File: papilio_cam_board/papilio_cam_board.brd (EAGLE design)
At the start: 68.4 x 68.6 mm, 20 parts, among them U2 V_REG_317SMD

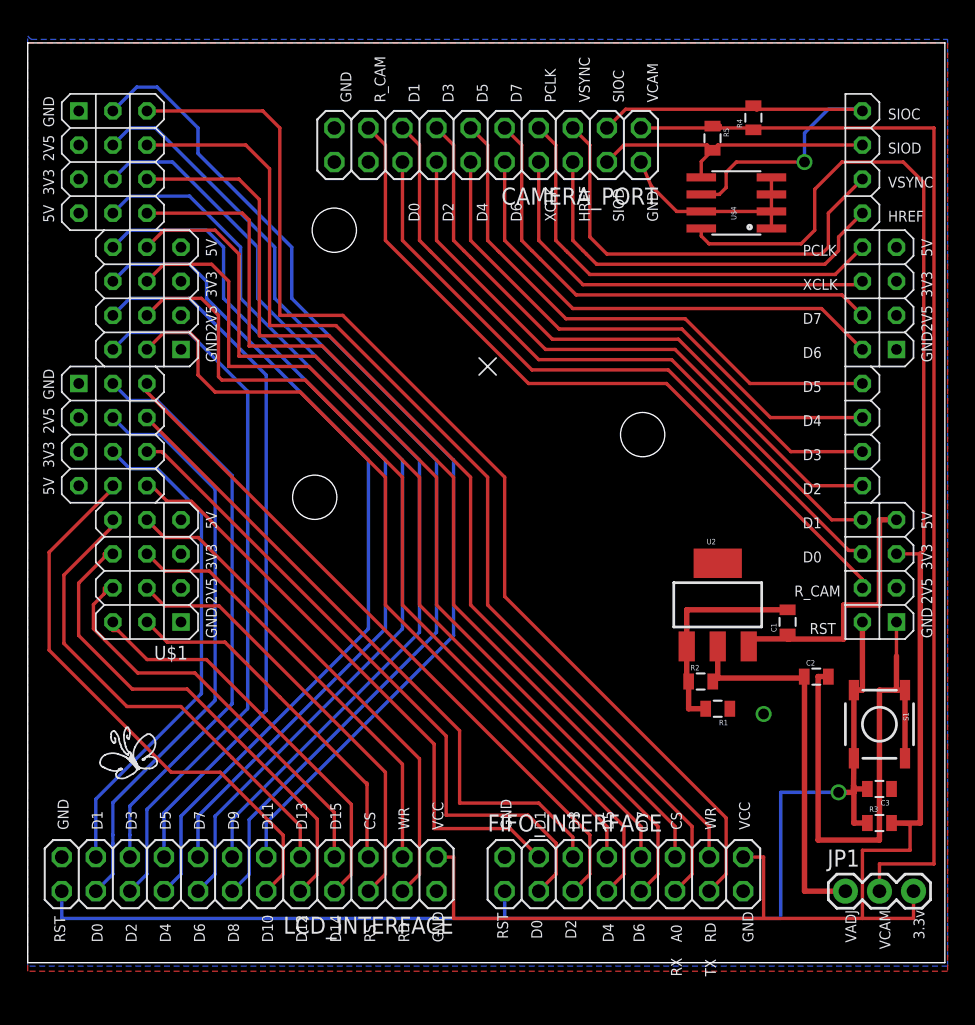
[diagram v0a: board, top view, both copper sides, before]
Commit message: adding papilio wing to support camera sensor and other ports
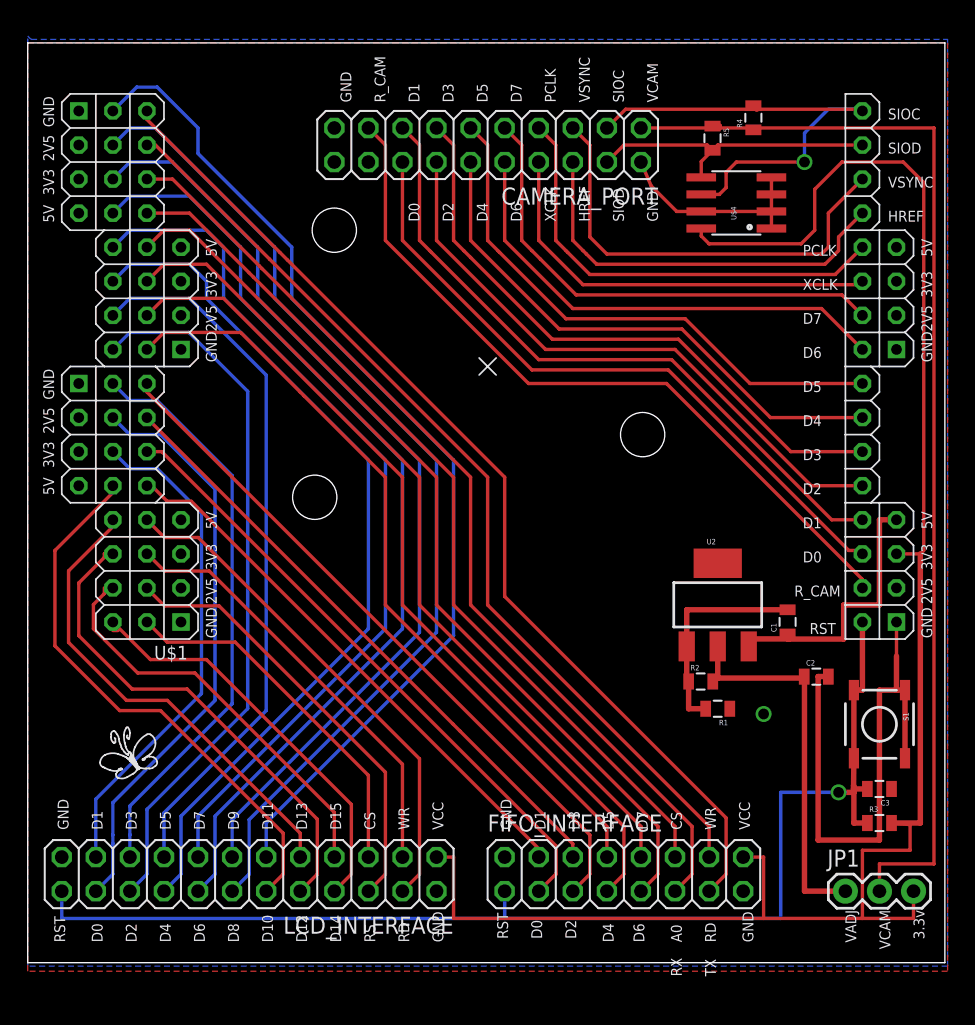
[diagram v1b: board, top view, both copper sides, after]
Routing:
- net FIFO_D0: track 84.4 -> 76.6 mm
- net FIFO_D1: track 77.7 -> 70.8 mm
- net FIFO_D2: track 77.5 -> 71.6 mm
- net FIFO_D3: track 71.7 -> 66.2 mm
- net FIFO_D4: track 72.4 -> 68.0 mm
- net FIFO_D5: track 66.3 -> 62.6 mm
- net FIFO_RD: track 50.2 -> 46.6 mm
- net FIFO_CS: track 49.5 -> 46.0 mm
- net FIFO_WR: track 44.4 -> 41.0 mm
- net FIFO_D6: track 66.2 -> 63.5 mm
- net FIFO_D7: track 59.4 -> 57.9 mm
- net LCD_D12: track 36.3 -> 35.5 mm
- net LCD_D11: track 42.1 -> 41.4 mm

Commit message: modifying design
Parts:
- added C4: (no value), SparkFun:0805
- added JP3: STAND-OFF, SparkFun:STAND-OFF
- added JP4: (no value), SparkFun:1X03
- moved R4 3.45 mm to (57.4, 64.0), turned to 0 degrees
- moved R5 2.90 mm to (49.3, 59.2)
- moved U$4 1.55 mm to (54.4, 56.4)
- moved R1 0.25 mm to (51.4, 18.7)
- moved R2 0.25 mm to (50.2, 20.7)
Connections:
- new net N$2: CAMERA_PORT.17, JP4.2
- net 3.3V: now also C4.2
- net GND: now also C4.1, JP4.3; no longer CAMERA_PORT.19
- net RESET_CAM: now also CAMERA_PORT.19, JP4.1; no longer CAMERA_PORT.17
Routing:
- net N$2: track 0.00 -> 18.5 mm
- net RESET_CAM: track 55.6 -> 65.6 mm
- net LCD_D06: track 65.6 -> 58.0 mm
- net LCD_D05: track 64.8 -> 57.7 mm
- net VCAM: track 83.6 -> 89.0 mm
- net LCD_D10: track 76.4 -> 71.9 mm
- net LCD_D09: track 75.6 -> 72.2 mm
- net LCD_D08: track 70.2 -> 67.3 mm
- net HREF: track 30.3 -> 33.2 mm
- net 3.3V: track 134.3 -> 137.1 mm
- net LCD_D11: track 41.4 -> 44.1 mm
- net PCLK: track 33.7 -> 36.2 mm
- net LCD_D07: track 70.9 -> 68.4 mm
- net VSYNC: track 33.8 -> 36.3 mm
- net LCD_D12: track 35.5 -> 37.9 mm
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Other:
- board size 68.4 x 68.6 mm -> 68.6 x 68.6 mm
- board text added: "OV7670"
- board text added: "OV7725"

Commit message: modifying design
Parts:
- moved JP1 60.7 mm to (59.7, 66.0)
- moved C2 21.4 mm to (40.1, 31.9), turned to 270 degrees
- moved R1 20.4 mm to (34.9, 30.6)
- moved R2 20.2 mm to (33.7, 32.4)
- moved C1 20.1 mm to (40.1, 36.8)
- moved U2 20.1 mm to (34.9, 38.1)
- moved R3 10.6 mm to (59.1, 20.1), turned to 90 degrees
- moved FIFO_INTERFACE 2.54 mm to (41.9, 6.60)
- moved C3 2.03 mm to (63.7, 15.0)
- moved S1 2.03 mm to (63.7, 19.8)
- moved R4 1.27 mm to (56.1, 64.0)
- renumbered U$1 to H
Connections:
- new net N$3: C3.2, R3.1, S1.4
- new net N$4: C3.1, S1.2
- net 3.3V: now also H.W2_3V3_2, H.W2_3V3_4
- net GND: no longer C3.1, S1.2
- net RESET: no longer C3.2, R3.1, S1.4
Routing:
- net 3.3V: track 137.1 -> 229.8 mm
- net VCAM: track 89.0 -> 28.4 mm
- net GND: track 55.9 -> 21.6 mm, vias 10 -> 9
- net VADJ: track 29.2 -> 53.3 mm, vias 0 -> 1
- net 5V: track 21.5 -> 39.3 mm
- net N$3: track 0.00 -> 7.84 mm
- net N$4: track 0.00 -> 3.29 mm
- net FIFO_D6: track 62.5 -> 61.3 mm
- net FIFO_D4: track 68.0 -> 67.0 mm
- net FIFO_D5: track 61.6 -> 60.6 mm
- net FIFO_D1: track 70.8 -> 69.8 mm
- net FIFO_D3: track 66.2 -> 65.2 mm
- net FIFO_D2: track 71.6 -> 70.6 mm
- net FIFO_D0: track 76.7 -> 75.6 mm
- net FIFO_WR: track 41.7 -> 40.7 mm
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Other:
- outline, holes or cut-outs redrawn
- board text added: "49387"
- board text removed: "3.3v"
- board text removed: "RX"
- board text removed: "TX"
- board text removed: "VADJ"

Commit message: reversing some changes
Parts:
- moved JP1 60.7 mm to (61.0, 5.33)
- moved C2 21.4 mm to (58.8, 21.3), turned to 0 degrees
- moved R1 20.4 mm to (51.4, 18.7)
- moved R2 20.2 mm to (50.2, 20.7)
- moved C1 20.1 mm to (56.7, 25.4)
- moved U2 20.1 mm to (51.4, 26.7)
- moved R3 10.6 mm to (63.5, 10.4), turned to 0 degrees
- moved FIFO_INTERFACE 2.54 mm to (44.5, 6.60)
- moved C3 2.03 mm to (63.5, 13.0)
- moved S1 2.03 mm to (63.5, 17.8)
- moved R4 1.14 mm to (57.1, 63.5), turned to 90 degrees
- renumbered H to U$1
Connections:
- removed net N$3: C3.2, R3.1, S1.4
- removed net N$4: C3.1, S1.2
- net GND: now also C3.1, S1.2
- net RESET: now also C3.2, R3.1, S1.4
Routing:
- net VCAM: track 28.4 -> 85.2 mm
- net GND: track 21.6 -> 55.9 mm, vias 9 -> 10
- net VADJ: track 53.3 -> 29.2 mm, vias 1 -> 0
- net 5V: track 39.3 -> 21.5 mm
- net N$3: track 7.84 -> 0.00 mm
- net N$4: track 3.29 -> 0.00 mm
- net 3.3V: track 229.8 -> 226.5 mm
- net SIOC: track 38.8 -> 37.5 mm
- net FIFO_D6: track 61.3 -> 62.5 mm
- net FIFO_D4: track 67.0 -> 68.0 mm
- net FIFO_D5: track 60.6 -> 61.6 mm
- net FIFO_D1: track 69.8 -> 70.8 mm
- net FIFO_D3: track 65.2 -> 66.2 mm
- net FIFO_D2: track 70.6 -> 71.6 mm
- net FIFO_D0: track 75.6 -> 76.7 mm
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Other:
- outline, holes or cut-outs redrawn
- board text added: "3.3v"
- board text added: "RX"
- board text added: "TX"
- board text added: "VADJ"
- board text removed: "49387"

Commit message: minor changes
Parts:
- moved FIFO_INTERFACE 2.54 mm to (47.0, 6.60)
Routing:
- net GND: track 55.9 -> 25.9 mm
- net A0: track 52.0 -> 55.0 mm
- net FIFO_CS: track 46.5 -> 48.6 mm
- net FIFO_RD: track 47.2 -> 49.1 mm
- net FIFO_WR: track 41.7 -> 43.6 mm
- net FIFO_D3: track 66.2 -> 67.3 mm
- net FIFO_D2: track 71.6 -> 72.7 mm
- net FIFO_D7: track 57.0 -> 58.0 mm
- net FIFO_D6: track 62.5 -> 63.6 mm
- net FIFO_D4: track 68.0 -> 69.1 mm
- net FIFO_D1: track 70.8 -> 71.9 mm
- net FIFO_D5: track 61.6 -> 62.7 mm
- net FIFO_D0: track 76.7 -> 77.7 mm

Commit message: refactoring
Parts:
- added JP6: (no value), SparkFun:1X03
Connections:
- new net ALIM_LCD: JP6.2, LCD_INTERFACE.1
- new net LCD_5V: JP6.1, U$1.W2_5V
- net 3.3V: now also JP6.3; no longer LCD_INTERFACE.1
- net GND: now also C1.2
- net N$1: no longer C1.2
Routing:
- net LCD_5V: track 0.00 -> 31.6 mm
- net N$1: track 16.4 -> 6.19 mm
- net 3.3V: track 226.5 -> 222.5 mm
- net ALIM_LCD: track 0.00 -> 2.72 mm
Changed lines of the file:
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@@
 <element name="JP4" library="SparkFun" package="1X03" value="" x="16.764" y="64.77" rot="R270"/>
 <element name="C4" library="SparkFun" package="0805" value="" x="54.356" y="52.578" rot="R180"/>
+<element name="JP6" library="SparkFun" package="1X03" value="" x="33.1978" y="10.414" rot="R270"/>
 </elements>
 <signals>
@@
 <contactref element="C4" pad="1"/>
 <via x="12.446" y="42.418" extent="1-16" drill="0.8"/>
-<via x="32.766" y="10.668" extent="1-16" drill="0.8"/>
+<via x="30.48" y="10.668" extent="1-16" drill="0.8"/>
 <via x="35.814" y="33.274" extent="1-16" drill="0.8"/>
 <via x="4.572" y="49.53" extent="1-16" drill="0.8"/>
@@
 <via x="19.558" y="59.436" extent="1-16" drill="0.8"/>
 <via x="5.842" y="18.288" extent="1-16" drill="0.8"/>
+<contactref element="C1" pad="2"/>
 </signal>
 <signal name="5V">
@@
 <contactref element="R3" pad="2"/>
 <contactref element="JP1" pad="3"/>
-<contactref element="LCD_INTERFACE" pad="1"/>
 <wire x1="64.4" y1="10.414" x2="66.548" y2="10.414" width="0.4064" layer="1"/>
 <wire x1="66.548" y1="10.414" x2="66.548" y2="30.48" width="0.4064" layer="1"/>
@@
 <wire x1="1.016" y1="8.636" x2="1.016" y2="4.318" width="0.254" layer="1"/>
 <wire x1="1.016" y1="4.318" x2="2.032" y2="3.302" width="0.254" layer="1"/>
-<wire x1="57.404" y1="3.302" x2="32.258" y2="3.302" width="0.254" layer="1"/>
-<wire x1="32.258" y1="3.302" x2="2.032" y2="3.302" width="0.254" layer="1"/>
-<wire x1="30.48" y1="7.874" x2="32.004" y2="7.874" width="0.254" layer="1"/>
-<wire x1="32.004" y1="7.874" x2="32.258" y2="7.62" width="0.254" layer="1"/>
-<wire x1="32.258" y1="7.62" x2="32.258" y2="3.302" width="0.254" layer="1"/>
+<wire x1="57.404" y1="3.302" x2="33.0962" y2="3.302" width="0.254" layer="1"/>
+<wire x1="33.0962" y1="3.302" x2="2.032" y2="3.302" width="0.254" layer="1"/>
 <wire x1="3.81" y1="38.1" x2="2.54" y2="38.1" width="0.254" layer="1"/>
 <wire x1="2.54" y1="38.1" x2="1.778" y2="38.862" width="0.254" layer="1"/>
+<contactref element="JP6" pad="3"/>
+<wire x1="33.1978" y1="5.334" x2="33.0962" y2="5.334" width="0.254" layer="1"/>
+<wire x1="33.0962" y1="5.334" x2="33.0962" y2="3.302" width="0.254" layer="1"/>
 </signal>
 <signal name="N$1">
@@
 <contactref element="R1" pad="2"/>
 <contactref element="R2" pad="1"/>
-<contactref element="C1" pad="2"/>
-<wire x1="56.651" y1="26.31" x2="49.1326" y2="26.31" width="0.4064" layer="1"/>
-<wire x1="49.1326" y1="26.31" x2="49.1326" y2="23.5812" width="0.4064" layer="1"/>
 <wire x1="49.274" y1="20.711" x2="49.1326" y2="21.219" width="0.4064" layer="1"/>
 <wire x1="49.1326" y1="21.219" x2="49.1326" y2="23.5812" width="0.4064" layer="1"/>
@@
 <wire x1="25.4" y1="63.5" x2="25.4" y2="62.23" width="0.254" layer="1"/>
 </signal>
+<signal name="ALIM_LCD">
+<contactref element="JP6" pad="2"/>
+<contactref element="LCD_INTERFACE" pad="1"/>
+<wire x1="33.1978" y1="7.874" x2="30.48" y2="7.874" width="0.254" layer="1"/>
+</signal>
+<signal name="LCD_5V">
+<contactref element="U$1" pad="W2_5V"/>
+<contactref element="JP6" pad="1"/>
+<wire x1="11.43" y1="33.02" x2="11.43" y2="32.1818" width="0.254" layer="1"/>
+<wire x1="11.43" y1="32.1818" x2="33.1978" y2="10.414" width="0.254" layer="1"/>
+</signal>
 </signals>
